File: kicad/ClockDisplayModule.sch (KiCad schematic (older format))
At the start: 5 parts, among them IC1 ATMEGA88PA-A, P101 CONN_02X03, P102 CONN_01X05

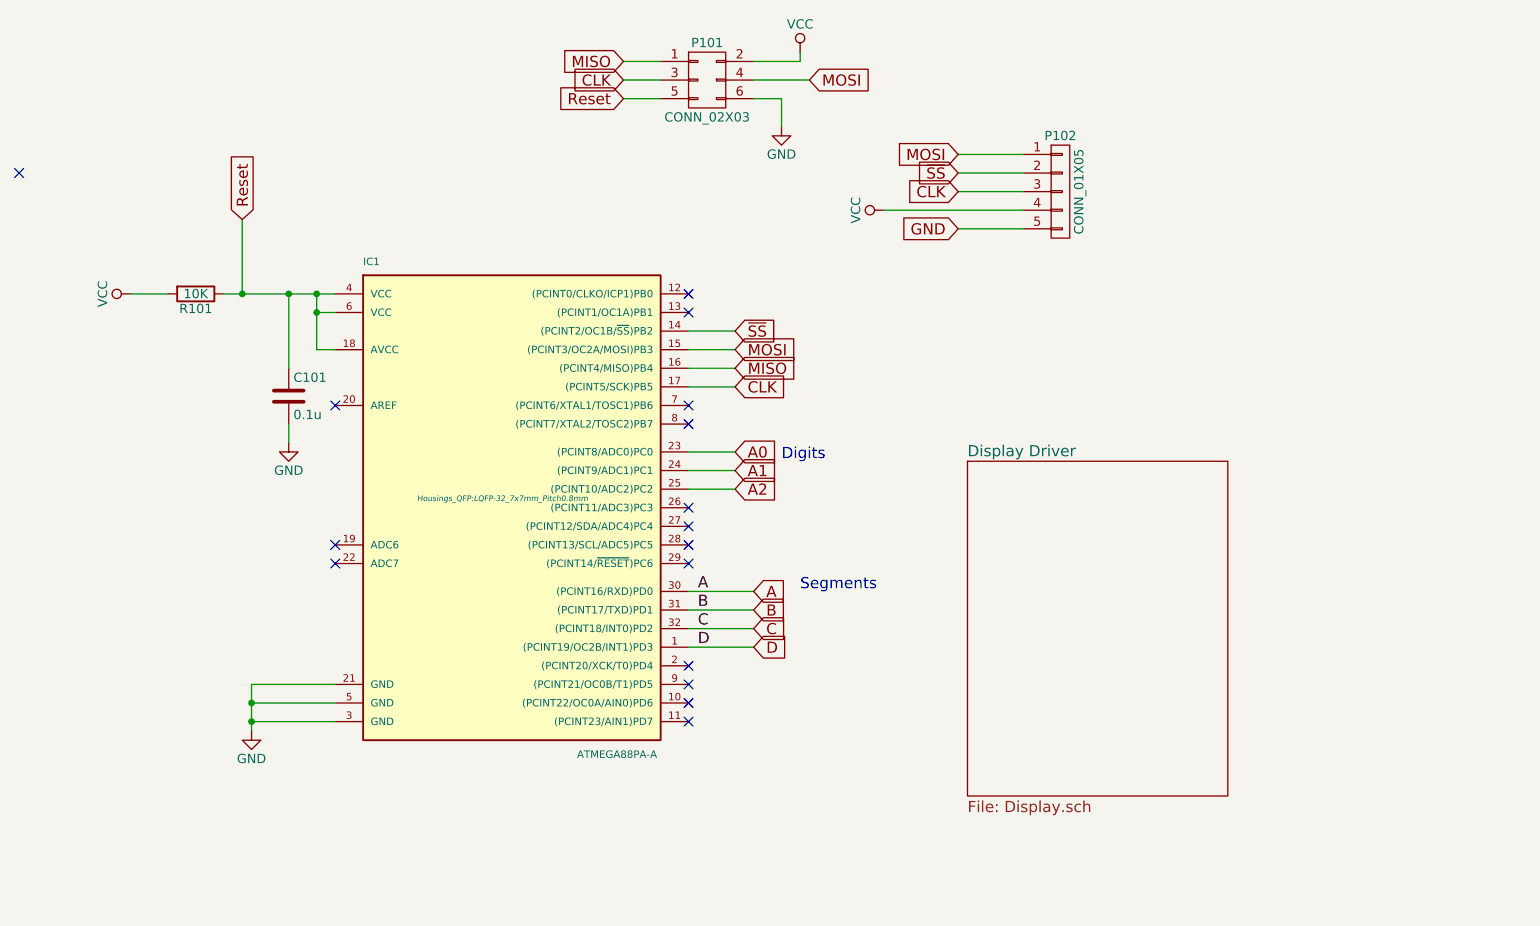
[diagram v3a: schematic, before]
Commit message: Updated main project with fixes from issues discovered when brining up the board
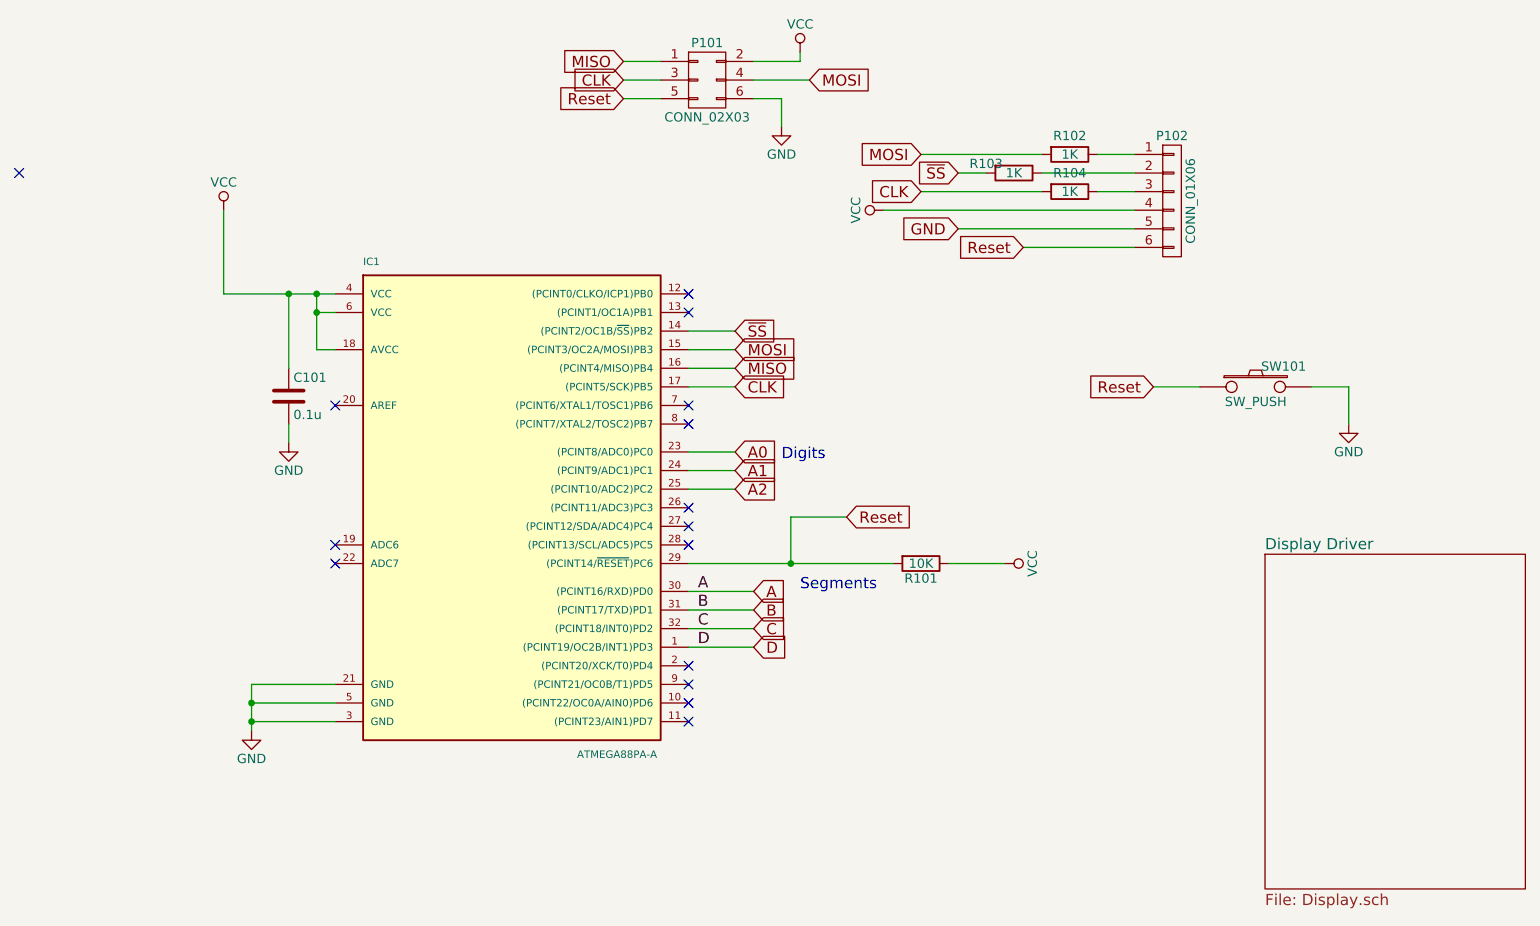
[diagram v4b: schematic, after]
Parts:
- removed P102: CONN_01X05, Pin_Headers:Pin_Header_Straight_1x05, symbol CONN_01X05
- added P102: CONN_01X06, Pin_Headers:Pin_Header_Straight_1x06, symbol CONN_01X06
- added R102, R103, R104: 1K, Resistors_SMD:R_0805, symbol R
- added SW101: SW_PUSH, ClockFootprints:PTS525SM15SMTR2LFS, symbol SW_PUSH
- C101: footprint Capacitors_SMD:C_0805_HandSoldering -> Capacitors_SMD:C_0805
- R101: footprint Resistors_SMD:R_0805_HandSoldering -> Resistors_SMD:R_0805
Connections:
- net CLK: now also R104.2
- net GND: now also P102.5 (P5), SW101.2
- net MOSI: now also R102.2
- net Reset: now also IC1.29 ((PCINT14/~RESET~)PC6), R101.2, P102.6 (P6), SW101.1; no longer C101.1, IC1.18 (AVCC), IC1.4 (VCC), IC1.6 (VCC), R101.1
- net VCC: now also C101.1, IC1.18 (AVCC), IC1.4 (VCC), IC1.6 (VCC), R101.1, P102.4 (P4); no longer R101.2
- net ~SS: now also R103.2
- new net: P102.1 (P1), R102.1
- new net: P102.2 (P2), R103.1
- new net: P102.3 (P3), R104.1
- no-connect marks 16 -> 15
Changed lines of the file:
@@
 $EndDescr
-$Comp
-L R R101
-U 1 1 5575BA42
-P 2100 2200
-F 0 "R101" V 2180 2200 50  0000 C CNN
-F 1 "10K" V 2100 2200 50  0000 C CNN
-F 2 "Resistors_SMD:R_0805_HandSoldering" V 2030 2200 30  0001 C CNN
-F 3 "" H 2100 2200 30  0000 C CNN
-	1    2100 2200
-	0    1    1    0
-$EndComp
 $Comp
 L C C101
@@
 F 0 "C101" H 2625 2850 50  0000 L CNN
 F 1 "0.1u" H 2625 2650 50  0000 L CNN
-F 2 "Capacitors_SMD:C_0805_HandSoldering" H 2638 2600 30  0001 C CNN
+F 2 "Capacitors_SMD:C_0805" H 2638 2600 30  0001 C CNN
 F 3 "" H 2600 2750 60  0000 C CNN
 	1    2600 2750
@@
 D
 NoConn ~ 4750 4400
-Text GLabel 6200 1450 0    60   Input ~ 0
+Text GLabel 6000 1450 0    60   Input ~ 0
 MOSI
 Text GLabel 6200 1550 0    60   Input ~ 0
 ~SS
-Text GLabel 6200 1650 0    60   Input ~ 0
+Text GLabel 6000 1650 0    60   Input ~ 0
 CLK
 Text GLabel 6200 1850 0    60   Input ~ 0
@@
 L VCC #PWR02
 U 1 1 558686BB
-P 1750 2200
-F 0 "#PWR02" H 1750 2050 50  0001 C CNN
-F 1 "VCC" H 1750 2350 50  0000 C CNN
-F 2 "" H 1750 2200 60  0000 C CNN
-F 3 "" H 1750 2200 60  0000 C CNN
-	1    1750 2200
-	0    -1   -1   0
+P 2250 1750
+F 0 "#PWR02" H 2250 1600 50  0001 C CNN
+F 1 "VCC" H 2250 1900 50  0000 C CNN
+F 2 "" H 2250 1750 60  0000 C CNN
+F 3 "" H 2250 1750 60  0000 C CNN
+	1    2250 1750
+	1    0    0    -1
 $EndComp
 $Comp
@@
 A2
 $Sheet
-S 6250 3100 1400 1800
+S 7850 3600 1400 1800
 U 5587144A
 F0 "Display Driver" 60
@@
 Text GLabel 4400 1150 0    60   Input ~ 0
 Reset
-Text GLabel 2350 1800 1    60   Input ~ 0
-Reset
-$Comp
-L CONN_01X05 P102
-U 1 1 5575F20D
-P 6750 1650
-F 0 "P102" H 6750 1950 50  0000 C CNN
-F 1 "CONN_01X05" V 6850 1650 50  0000 C CNN
-F 2 "Pin_Headers:Pin_Header_Straight_1x05" H 6750 1650 60  0001 C CNN
-F 3 "" H 6750 1650 60  0000 C CNN
-	1    6750 1650
-	1    0    0    -1
-$EndComp
 Text GLabel 5000 2600 2    60   Input ~ 0
 MISO
@@
 F 0 "IC1" H 3000 4550 40  0000 L BNN
 F 1 "ATMEGA88PA-A" H 4150 1900 40  0000 L BNN
-F 2 "Housings_QFP:LQFP-32_7x7mm_Pitch0.8mm" H 3750 3300 30  0000 C CIN
+F 2 "Housings_QFP:LQFP-32_7x7mm_Pitch0.8mm" H 3750 3300 30  0001 C CIN
 F 3 "" H 3750 3300 60  0000 C CNN
 	1    3750 3300
@@
 	4750 4100 5100 4100
 Wire Wire Line
-	6200 1450 6550 1450
-Wire Wire Line
-	6200 1550 6550 1550
-Wire Wire Line
-	6200 1650 6550 1650
-Wire Wire Line
-	5800 1750 6550 1750
-Wire Wire Line
-	6200 1850 6550 1850
+	5800 1750 7150 1750
+Wire Wire Line
+	6200 1850 7150 1850
 Wire Wire Line
 	5000 3050 4750 3050
@@
 Connection ~ 2750 2200
 Wire Wire Line
-	1750 2200 1950 2200
-Wire Wire Line
 	2250 2200 2850 2200
 Wire Wire Line
@@
 	2600 2600 2600 2200
 Connection ~ 2600 2200
-Wire Wire Line
-	2350 1800 2350 2200
-Connection ~ 2350 2200
 NoConn ~ 2850 2800
 NoConn ~ 4750 2200
@@
 NoConn ~ 4750 3450
 NoConn ~ 4750 3550
-NoConn ~ 4750 3650
 NoConn ~ 1150 1550
+Text GLabel 5600 3400 2    60   Input ~ 0
+Reset
+Wire Wire Line
+	4750 3650 5850 3650
+Wire Wire Line
+	5300 3650 5300 3400
+Wire Wire Line
+	5300 3400 5600 3400
+$Comp
+L R R101
+U 1 1 5660E01D
+P 6000 3650
+F 0 "R101" V 6080 3650 50  0000 C CNN
+F 1 "10K" V 6000 3650 50  0000 C CNN
+F 2 "Resistors_SMD:R_0805" V 5930 3650 30  0001 C CNN
+F 3 "" H 6000 3650 30  0000 C CNN
+	1    6000 3650
+	0    1    1    0
+$EndComp
+Connection ~ 5300 3650
+$Comp
+L VCC #PWR07
+U 1 1 5660E0C5
+P 6450 3650
+F 0 "#PWR07" H 6450 3500 50  0001 C CNN
+F 1 "VCC" H 6450 3800 50  0000 C CNN
+F 2 "" H 6450 3650 60  0000 C CNN
+F 3 "" H 6450 3650 60  0000 C CNN
+	1    6450 3650
+	0    1    1    0
+$EndComp
+Wire Wire Line
+	6450 3650 6150 3650
+$Comp
+L R R102
+U 1 1 5660E284
+P 6800 1450
+F 0 "R102" V 6700 1450 50  0000 C CNN
+F 1 "1K" V 6800 1450 50  0000 C CNN
+F 2 "Resistors_SMD:R_0805" V 6730 1450 30  0001 C CNN
+F 3 "" H 6800 1450 30  0000 C CNN
+	1    6800 1450
+	0    1    1    0
+$EndComp
+$Comp
+L R R103
+U 1 1 5660E384
+P 6500 1550
+F 0 "R103" V 6450 1400 50  0000 C CNN
+F 1 "1K" V 6500 1550 50  0000 C CNN
+F 2 "Resistors_SMD:R_0805" V 6430 1550 30  0001 C CNN
+F 3 "" H 6500 1550 30  0000 C CNN
+	1    6500 1550
+	0    1    1    0
+$EndComp
+$Comp
+L R R104
+U 1 1 5660E3C8
+P 6800 1650
+F 0 "R104" V 6700 1650 50  0000 C CNN
+F 1 "1K" V 6800 1650 50  0000 C CNN
+F 2 "Resistors_SMD:R_0805" V 6730 1650 30  0001 C CNN
+F 3 "" H 6800 1650 30  0000 C CNN
+	1    6800 1650
+	0    1    1    0
+$EndComp
+Wire Wire Line
+	6000 1450 6650 1450
+Wire Wire Line
+	6950 1450 7150 1450
+Wire Wire Line
+	7150 1550 6650 1550
+Wire Wire Line
+	6350 1550 6200 1550
+Wire Wire Line
+	6000 1650 6650 1650
+Wire Wire Line
+	6950 1650 7150 1650
+$Comp
+L CONN_01X06 P102
+U 1 1 5660E685
+P 7350 1700
+F 0 "P102" H 7350 2050 50  0000 C CNN
+F 1 "CONN_01X06" V 7450 1700 50  0000 C CNN
+F 2 "Pin_Headers:Pin_Header_Straight_1x06" H 7350 1700 60  0001 C CNN
+F 3 "" H 7350 1700 60  0000 C CNN
+	1    7350 1700
+	1    0    0    -1
+$EndComp
+Text GLabel 6550 1950 0    60   Input ~ 0
+Reset
+Wire Wire Line
+	6550 1950 7150 1950
+Wire Wire Line
+	2250 1750 2250 2200
+$Comp
+L SW_PUSH SW101
+U 1 1 5660EB7E
+P 7800 2700
+F 0 "SW101" H 7950 2810 50  0000 C CNN
+F 1 "SW_PUSH" H 7800 2620 50  0000 C CNN
+F 2 "ClockFootprints:PTS525SM15SMTR2LFS" H 7800 2700 60  0001 C CNN
+F 3 "" H 7800 2700 60  0000 C CNN
+	1    7800 2700
+	1    0    0    -1
+$EndComp
+Text GLabel 7250 2700 0    60   Input ~ 0
+Reset
+$Comp
+L GND #PWR08
+U 1 1 5660EC1F
+P 8300 2900
+F 0 "#PWR08" H 8300 2650 50  0001 C CNN
+F 1 "GND" H 8300 2750 50  0000 C CNN
+F 2 "" H 8300 2900 60  0000 C CNN
+F 3 "" H 8300 2900 60  0000 C CNN
+	1    8300 2900
+	1    0    0    -1
+$EndComp
+Wire Wire Line
+	7250 2700 7500 2700
+Wire Wire Line
+	8100 2700 8300 2700
+Wire Wire Line
+	8300 2700 8300 2900
 $EndSCHEMATC
